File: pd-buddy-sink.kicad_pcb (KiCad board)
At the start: 4 copper layers, 30 x 25 mm, 43 parts, among them J1 5-20 V⎓, P1 12401610E4#2A, P2 SWD, Q1 MMBT2222ALT1G, Q2 DMP4015SSS, SW1 Boot, SW2 Setup, U1 AP2204R-3.3TRG1, U2 STM32F072C8Ux, U3 FUSB302B

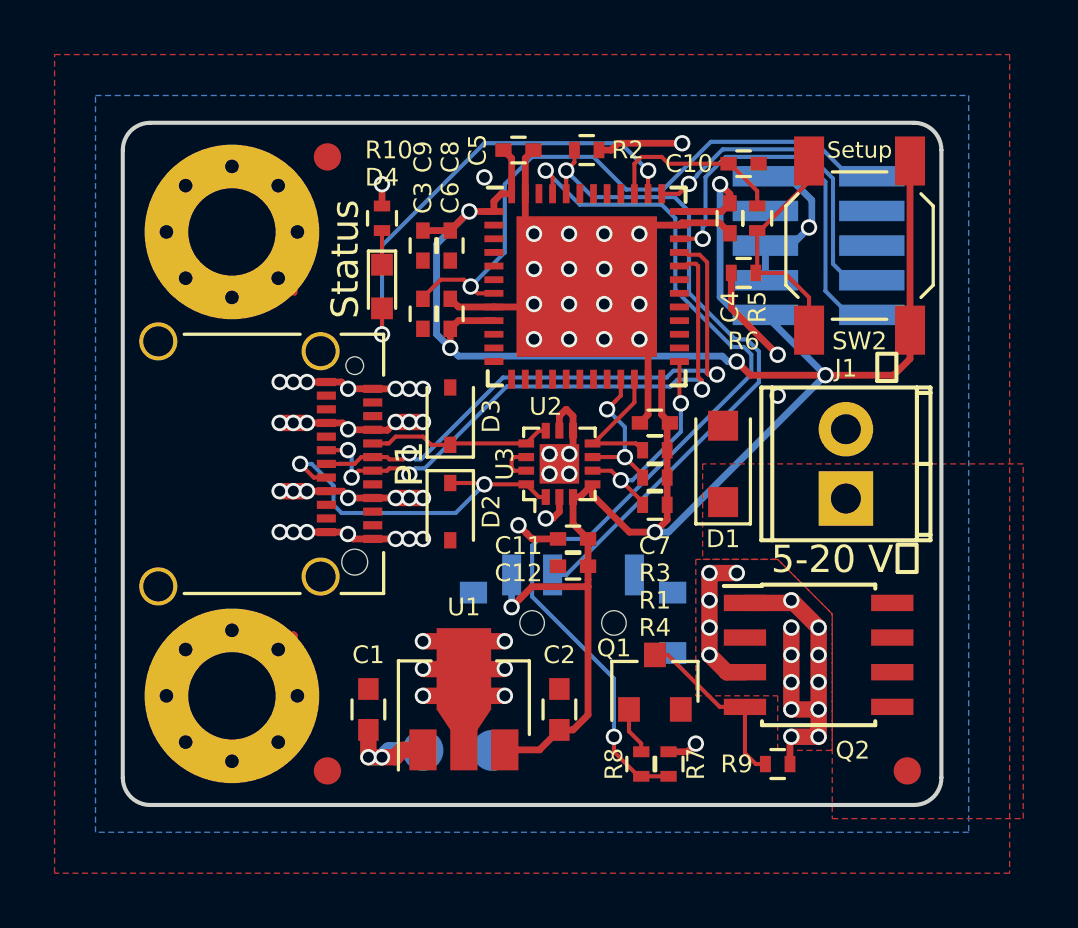
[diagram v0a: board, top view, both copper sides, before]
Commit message: Added fiducial refs, moved some other refs around
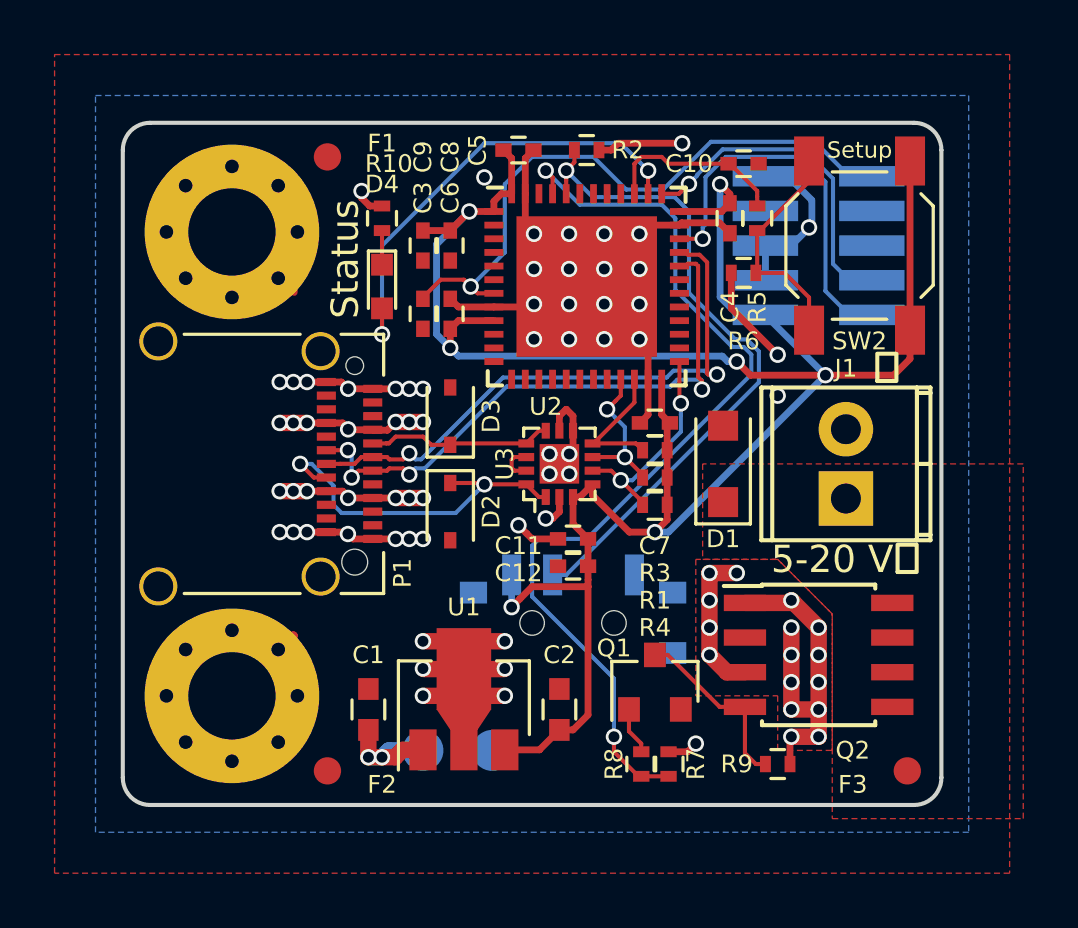
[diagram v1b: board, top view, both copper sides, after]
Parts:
- renumbered FID1 to F1, FID2 to F2, FID3 to F3
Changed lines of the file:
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@@
     (thickness 1.6)
     (drawings 10)
-    (tracks 529)
+    (tracks 531)
     (zones 0)
     (modules 43)
@@
     (tags marker)
     (attr virtual)
-    (fp_text reference FID3 (at 3.4 0.7) (layer F.SilkS) hide
-      (effects (font (size 1 1) (thickness 0.15)))
+    (fp_text reference F3 (at -2 0.5) (layer F.SilkS)
+      (effects (font (size 0.65 0.65) (thickness 0.12)))
     )
     (fp_text value Fiducial_1mm_Dia_2.54mm_Outer_CopperTop (at 0 -1.8) (layer F.Fab)
@@
     (tags marker)
     (attr virtual)
-    (fp_text reference FID2 (at 3.4 0.7) (layer F.SilkS) hide
-      (effects (font (size 1 1) (thickness 0.15)))
+    (fp_text reference F2 (at 2 0.5) (layer F.SilkS)
+      (effects (font (size 0.65 0.65) (thickness 0.12)))
     )
     (fp_text value Fiducial_1mm_Dia_2.54mm_Outer_CopperTop (at 0 -1.8) (layer F.Fab)
@@
     (tags "LED led 0603 SMD smd SMT smt smdled SMDLED smtled SMTLED")
     (attr smd)
-    (fp_text reference D4 (at -4 0 360) (layer F.SilkS)
+    (fp_text reference D4 (at -3.75 0 360) (layer F.SilkS)
       (effects (font (size 0.65 0.65) (thickness 0.12)))
     )
@@
     (tags "resistor 0402")
     (attr smd)
-    (fp_text reference R10 (at 2.5 0.25 180) (layer F.SilkS)
+    (fp_text reference R10 (at 2 0.25 180) (layer F.SilkS)
       (effects (font (size 0.65 0.65) (thickness 0.12)))
     )
@@
     (at 90 70 270)
     (attr smd)
-    (fp_text reference P1 (at 0 -2 270) (layer F.SilkS)
-      (effects (font (size 1 1) (thickness 0.15)))
+    (fp_text reference P1 (at 4 -1.75 270) (layer F.SilkS)
+      (effects (font (size 0.65 0.65) (thickness 0.12)))
     )
     (fp_text value 12401610E4#2A (at 0 10.5 270) (layer F.Fab)
@@
     (tags marker)
     (attr virtual)
-    (fp_text reference FID1 (at 3.4 0.7) (layer F.SilkS) hide
-      (effects (font (size 1 1) (thickness 0.15)))
+    (fp_text reference F1 (at 2 -0.5) (layer F.SilkS)
+      (effects (font (size 0.65 0.65) (thickness 0.12)))
     )
     (fp_text value Fiducial_1mm_Dia_2.54mm_Outer_CopperTop (at 0 -1.8) (layer F.Fab)
@@
   (segment (start 88.96 68.5) (end 88.25 68.5) (width 0.25) (layer F.Cu) (net 1))
   (via (at 88.25 68.5) (size 0.6) (drill 0.4) (layers F.Cu B.Cu) (net 1))
+  (segment (start 91 60.55) (end 90.55 60.55) (width 0.25) (layer F.Cu) (net 2))
+  (segment (start 90.25 60.25) (end 90.25 60.000086) (width 0.25) (layer F.Cu) (net 2))
+  (segment (start 90.55 60.55) (end 90.25 60.25) (width 0.25) (layer F.Cu) (net 2))
+  (via (at 90.25 60.000086) (size 0.6) (drill 0.4) (layers F.Cu B.Cu) (net 2))
   (segment (start 85.5 61.5) (end 86.365802 61.5) (width 0.25) (layer F.Cu) (net 2))
   (segment (start 86.365802 61.5) (end 87.782057 62.916255) (width 0.25) (layer F.Cu) (net 2))
@@
   (via (at 102 58.25) (size 0.6) (drill 0.4) (layers F.Cu B.Cu) (net 2))
   (segment (start 105.05 62) (end 105.05 63.27) (width 0.25) (layer B.Cu) (net 2))
-  (segment (start 91 60.55) (end 91 59.75) (width 0.25) (layer F.Cu) (net 2))
-  (via (at 91 59.75) (size 0.6) (drill 0.4) (layers F.Cu B.Cu) (net 2))
   (segment (start 95.1 64.25) (end 93.8 64.25) (width 0.25) (layer F.Cu) (net 2))
   (segment (start 93.8 64.25) (end 93.5 63.95) (width 0.25) (layer F.Cu) (net 2))

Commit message: 0.15 mm annular rings
Now the board is within spec for MacroFab.  Also, the power traces at
the USB connector are thicker, so should be able to carry high currents
more easily.
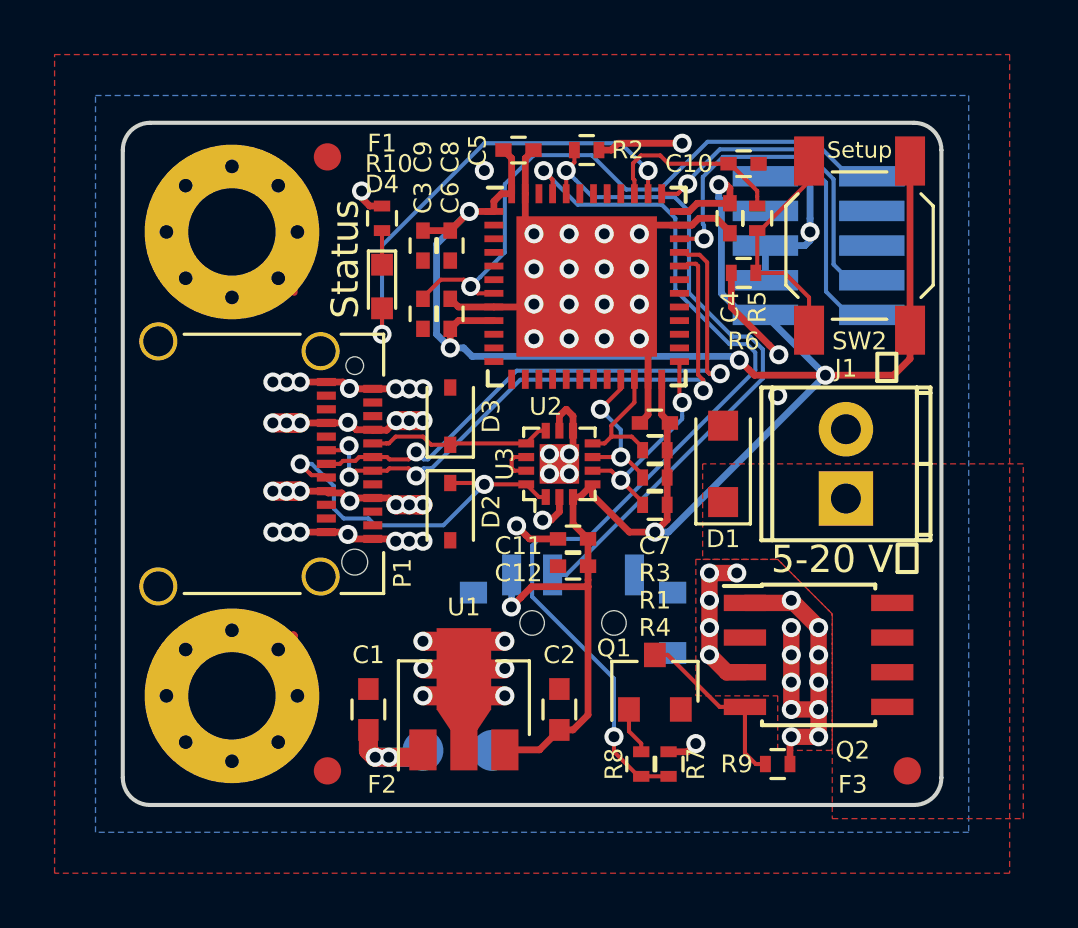
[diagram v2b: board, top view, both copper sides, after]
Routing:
- net VBUS: track 36.2 -> 37.8 mm
- net GND: track 68.4 -> 70.0 mm
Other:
- net class Default: via_dia 0.6 -> 0.7
- net class Power: trace_width 0.6 -> 0.7; via_dia 0.6 -> 0.7
- net class Power_Small: via_dia 0.6 -> 0.7

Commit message: Changed R10 to 220 Ω
It'll make the LED a bit brighter, and it's a more common value.
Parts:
- R10: value 300Ω -> 220Ω
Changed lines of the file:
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@@
     (links 138)
     (no_connects 0)
-    (area 72.101904 55 127.148096 85.71)
+    (area 81.424999 57.424999 111.575001 82.575001)
     (thickness 1.6)
     (drawings 10)
@@
       (effects (font (size 0.65 0.65) (thickness 0.12)))
     )
-    (fp_text value 300Ω (at 0 1.45 90) (layer F.Fab)
-      (effects (font (size 1 1) (thickness 0.15)))
-    )
+    (fp_text value 220Ω (at 0 1.45 90) (layer F.Fab)
+      (effects (font (size 1 1) (thickness 0.15)))
+    )

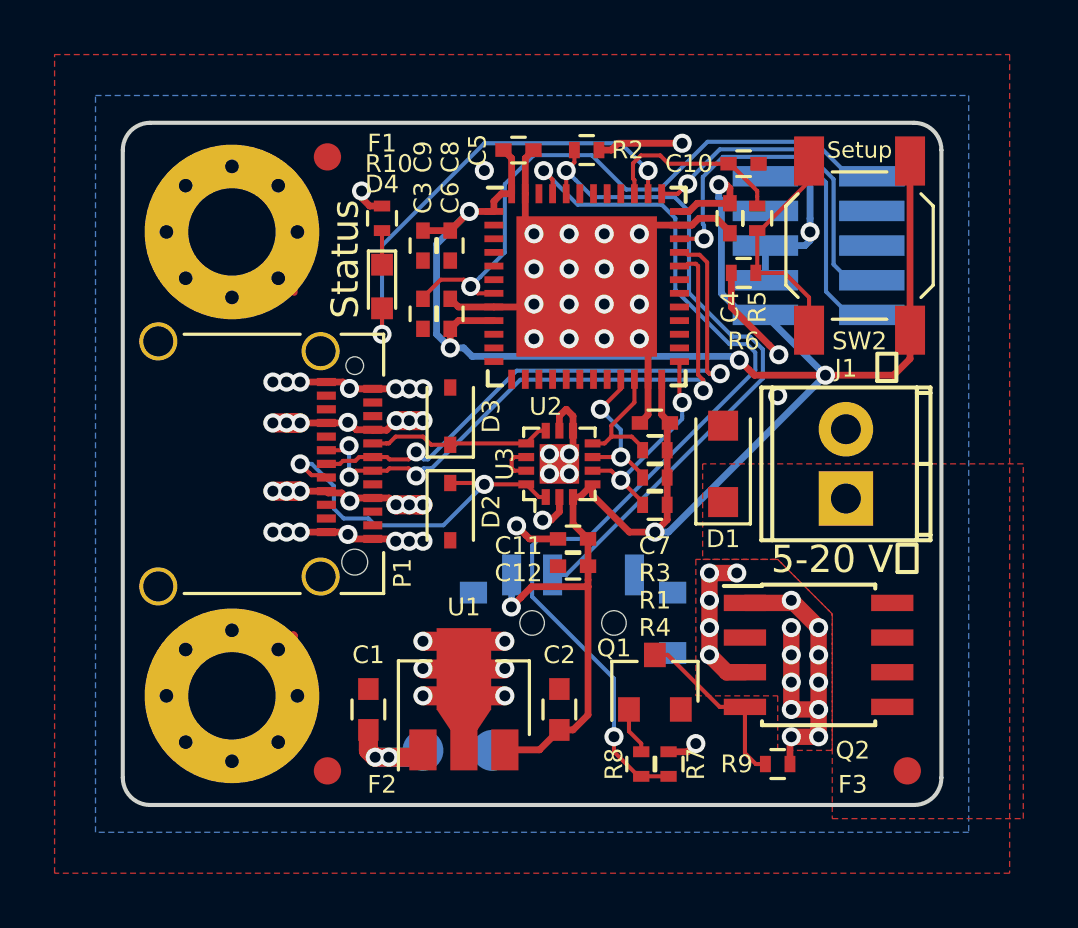
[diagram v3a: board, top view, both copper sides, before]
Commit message: Use FUSB302BMPX from standard kicad-library
Now that the appropriate pull requests have been merged, I can use the
standard part rather than the one I created in this repository.
Speaking of which, this commit removes FUSB302B and MLP-14 from this
repository.
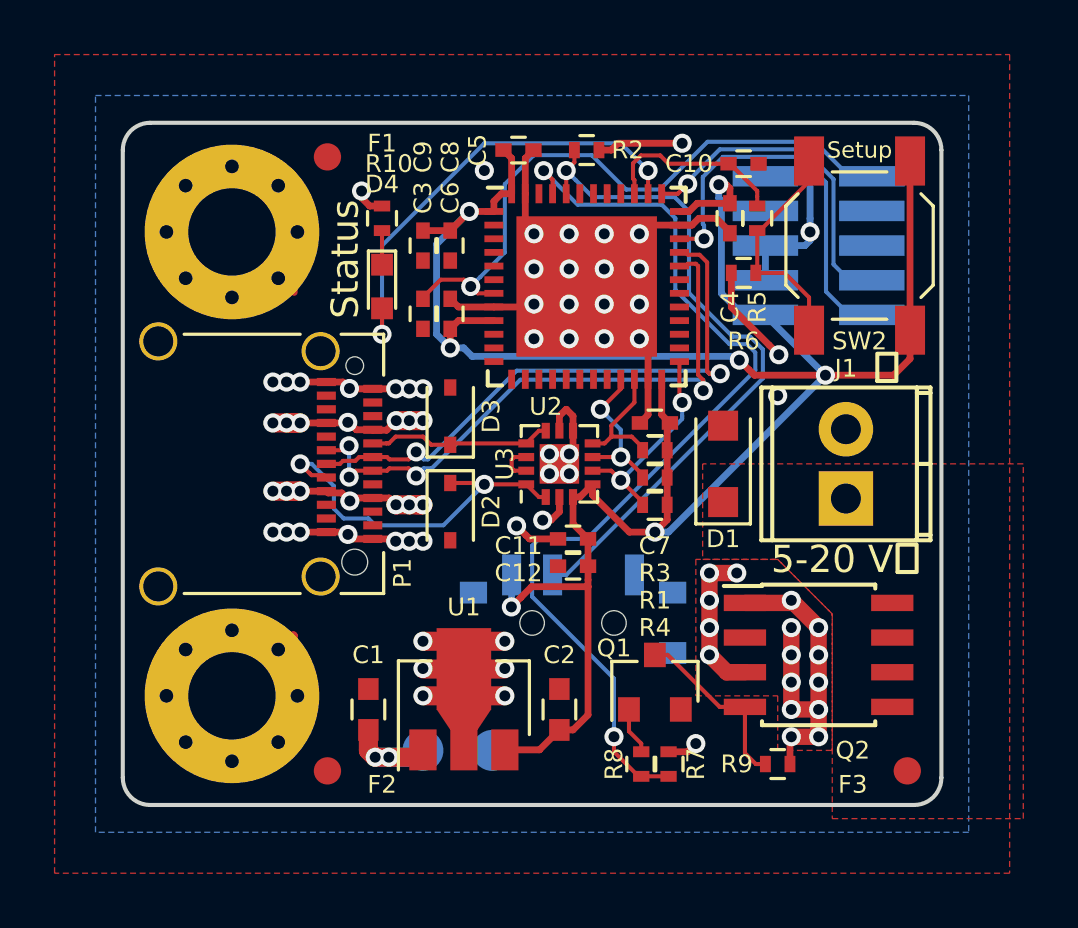
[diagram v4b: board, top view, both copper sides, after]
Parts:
- U3: value FUSB302B -> FUSB302BMPX; footprint pd-buddy:MLP-14 -> Housings_DFN_QFN:Fairchild_MLP14D
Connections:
- U3 pad 12: VCONN -> Net-(U3-Pad12)
- U3 pad 13: VCONN -> Net-(U3-Pad13)
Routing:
- net VCONN: track 1.46 -> 0.00 mm
- net Net-(U3-Pad13): track 0.00 -> 1.02 mm

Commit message: Use new USB Type-C schematic symbol
The footprints haven't been merged yet, but the symbol has.  Therefore,
I updated the footprint in the pd-buddy library to match the new symbol
(changed shield pin number to S1) and changed the schematic to have the
new connector symbol.  The board looks the same except that a couple
references changed.
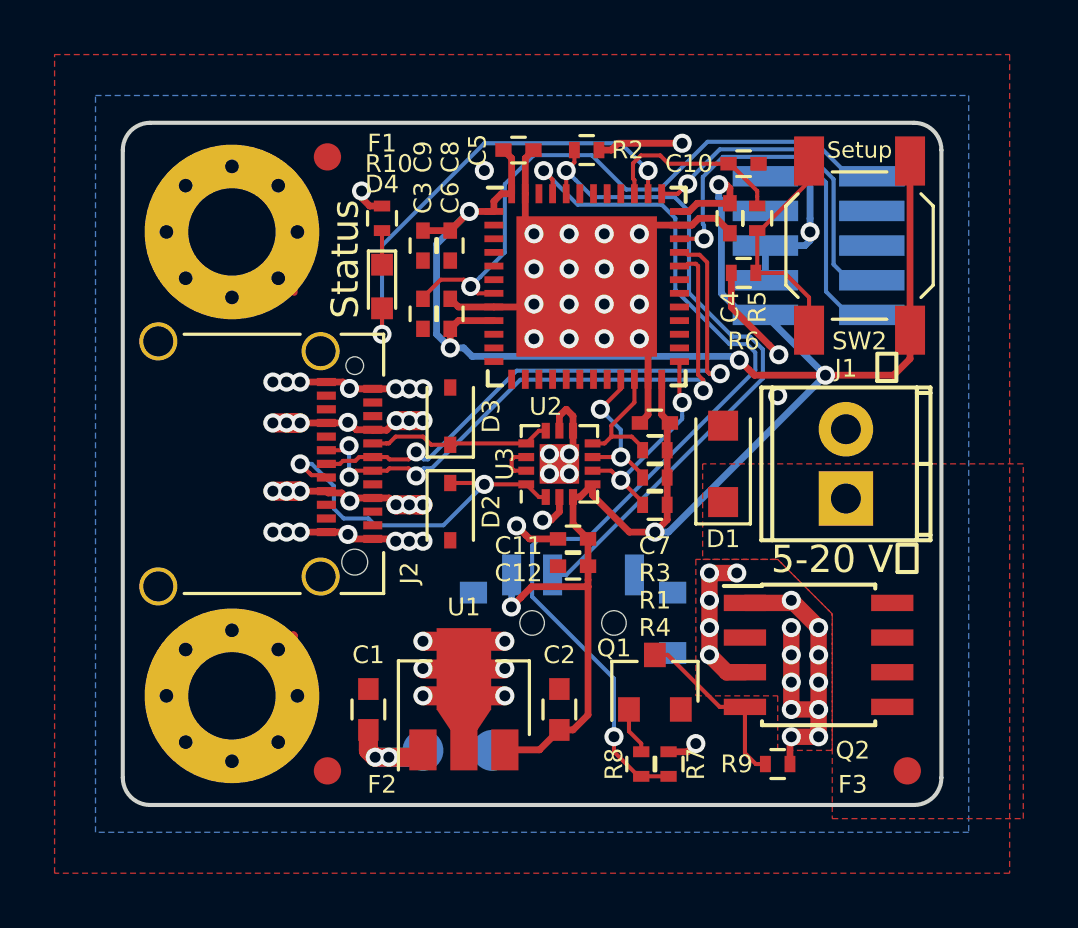
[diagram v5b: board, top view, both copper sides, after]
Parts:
- removed P2: SWD, pd-buddy:Pin_Header_Straight_2x05_Pitch1.27mm_SMD_NOPASTE
- added J2: USB_C_Receptacle, pd-buddy:Amphenol-12401610E4#2A, F.Cu at (90.0, 70.0)
- P1: value 12401610E4#2A -> SWD; footprint pd-buddy:Amphenol-12401610E4#2A -> pd-buddy:Pin_Header_Straight_2x05_Pitch1.27mm_SMD_NOPASTE; moved to B.Cu
- moved P1 18.8 mm to (107.0, 62.0), turned to 0 degrees
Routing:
- net Net-(U3-Pad13): track 1.02 -> 0.44 mm
- net Net-(U3-Pad12): track 0.44 -> 1.02 mm

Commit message: SOD-323F footprint for D2 and D3
KiCad has the right footprint now, so I don't have to substitute an
SOD-323 footprint.  The 3D model looks less inaccurate I suppose, but
still not right for the particular diodes I'm using.
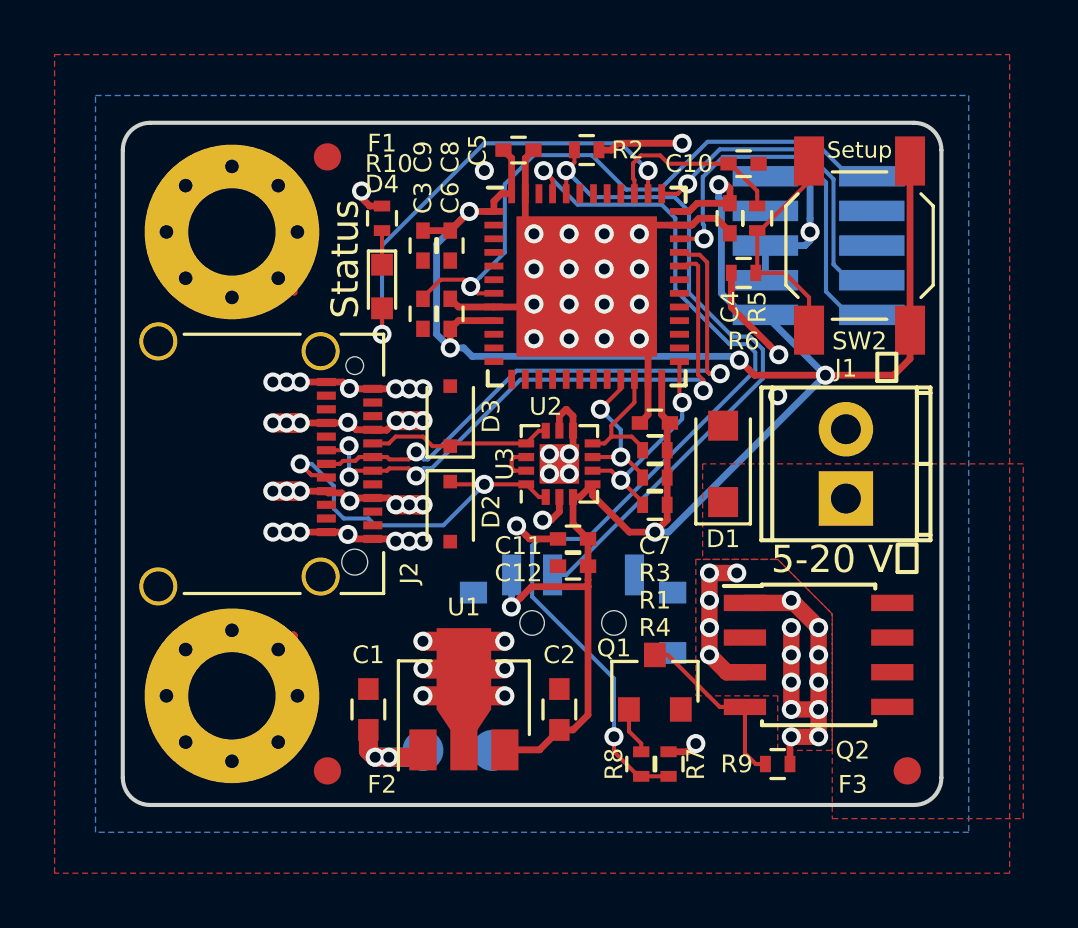
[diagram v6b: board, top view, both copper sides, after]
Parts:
- D2, D3: footprint Diodes_SMD:D_SOD-323 -> Diodes_SMD:D_SOD-323F
